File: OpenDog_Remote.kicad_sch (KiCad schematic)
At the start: 37 parts, among them J1 Conn_01x03_Pin, J10 Conn_01x03_Pin, J11 Conn_01x03_Pin, J12 Conn_01x02_Pin, J13 Conn_01x03_Pin, J14 Conn_01x03_Pin, J15 Conn_01x03_Pin, J16 Conn_01x03_Pin, J17 NRF, J18 Conn_02x08_Odd_Even, J2 Conn_01x03_Pin, J3 Conn_01x03_Pin, J4 Conn_01x03_Pin, J5 Conn_01x03_Pin, J6 Conn_01x03_Pin, J7 Conn_01x14, J8 Conn_01x03_Pin, J9 Conn_01x03_Pin, U1 Teensy4.1

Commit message: Added JLCPCB part #, round some board corners.
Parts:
- J1, J10, J11, J13, J14, J15, J16, J2, J3, J4, J5, J6, J8, J9: JLC Part # (none) -> C722693
- J12: JLC Part # (none) -> C2908596
- J18: JLC Part # (none) -> C92267
- J7: JLC Part # (none) -> C225266
- R1, R10, R11, R12, R13, R2, R3, R4, R5, R6, R7, R8, R9: JLC Part # (none) -> C25744
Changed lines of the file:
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@@
+      (effects (font (size 1.27 1.27)) hide)
+    )
+    (property "JLC Part #" "C722693" (at 66.04 149.225 0)
       (effects (font (size 1.27 1.27)) hide)
     )
@@
       (effects (font (size 1.27 1.27)) hide)
     )
+    (property "JLC Part #" "C25744" (at 90.17 139.7 0)
+      (effects (font (size 1.27 1.27)) hide)
+    )
     (pin "1")
     (pin "2")
@@
       (effects (font (size 1.27 1.27)) hide)
     )
+    (property "JLC Part #" "C722693" (at 207.01 44.45 0)
+      (effects (font (size 1.27 1.27)) hide)
+    )
     (pin "1")
     (pin "2")
@@
       (effects (font (size 1.27 1.27)) hide)
     )
+    (property "JLC Part #" "C25744" (at 88.9 173.99 0)
+      (effects (font (size 1.27 1.27)) hide)
+    )
     (pin "1")
     (pin "2")
@@
       (effects (font (size 1.27 1.27)) hide)
     )
+    (property "JLC Part #" "C25744" (at 55.245 173.99 0)
+      (effects (font (size 1.27 1.27)) hide)
+    )
     (pin "1")
     (pin "2")
@@
       (effects (font (size 1.27 1.27)) hide)
     )
+    (property "JLC Part #" "C25744" (at 152.4 173.99 0)
+      (effects (font (size 1.27 1.27)) hide)
+    )
     (pin "1")
     (pin "2")
@@
       (effects (font (size 1.27 1.27)) hide)
     )
+    (property "JLC Part #" "C25744" (at 121.92 139.7 0)
+      (effects (font (size 1.27 1.27)) hide)
+    )
     (pin "1")
     (pin "2")
@@
       (effects (font (size 1.27 1.27)) hide)
     )
+    (property "JLC Part #" "C25744" (at 122.555 182.88 0)
+      (effects (font (size 1.27 1.27)) hide)
+    )
     (pin "1")
     (pin "2")
@@
       (effects (font (size 1.27 1.27)) hide)
     )
+    (property "JLC Part #" "C722693" (at 206.375 99.06 0)
+      (effects (font (size 1.27 1.27)) hide)
+    )
     (pin "1")
     (pin "2")
@@
       (effects (font (size 1.27 1.27)) hide)
     )
+    (property "JLC Part #" "C722693" (at 134.62 181.61 0)
+      (effects (font (size 1.27 1.27)) hide)
+    )
     (pin "1")
     (pin "2")
@@
     )
     (property "Datasheet" "~" (at 36.195 48.26 0)
+      (effects (font (size 1.27 1.27)) hide)
+    )
+    (property "JLC Part #" "C92267" (at 36.195 48.26 0)
       (effects (font (size 1.27 1.27)) hide)
     )
@@
       (effects (font (size 1.27 1.27)) hide)
     )
+    (property "JLC Part #" "C722693" (at 206.375 90.805 0)
+      (effects (font (size 1.27 1.27)) hide)
+    )
     (pin "1")
     (pin "2")
@@
       (effects (font (size 1.27 1.27)) hide)
     )
+    (property "JLC Part #" "C25744" (at 55.245 182.88 0)
+      (effects (font (size 1.27 1.27)) hide)
+    )
     (pin "1")
     (pin "2")
@@
       (effects (font (size 1.27 1.27)) hide)
     )
+    (property "JLC Part #" "C25744" (at 26.035 140.97 0)
+      (effects (font (size 1.27 1.27)) hide)
+    )
     (pin "1")
     (pin "2")
@@
       (effects (font (size 1.27 1.27)) hide)
     )
+    (property "JLC Part #" "C25744" (at 58.42 140.335 0)
+      (effects (font (size 1.27 1.27)) hide)
+    )
     (pin "1")
     (pin "2")
@@
       (effects (font (size 1.27 1.27)) hide)
     )
+    (property "JLC Part #" "C722693" (at 129.54 148.59 0)
+      (effects (font (size 1.27 1.27)) hide)
+    )
     (pin "1")
     (pin "2")
@@
     )
     (property "Datasheet" "~" (at 97.79 148.59 0)
+      (effects (font (size 1.27 1.27)) hide)
+    )
+    (property "JLC Part #" "C722693" (at 97.79 148.59 0)
       (effects (font (size 1.27 1.27)) hide)
     )
@@
       (effects (font (size 1.27 1.27)) hide)
     )
+    (property "JLC Part #" "C722693" (at 33.655 149.86 0)
+      (effects (font (size 1.27 1.27)) hide)
+    )
     (pin "1")
     (pin "2")
@@
     )
     (property "Datasheet" "~" (at 201.295 131.445 0)
+      (effects (font (size 1.27 1.27)) hide)
+    )
+    (property "JLC Part #" "C225266" (at 201.295 131.445 0)
       (effects (font (size 1.27 1.27)) hide)
     )
@@
       (effects (font (size 1.27 1.27)) hide)
     )
+    (property "JLC Part #" "C722693" (at 206.375 82.55 0)
+      (effects (font (size 1.27 1.27)) hide)
+    )
     (pin "1")
     (pin "2")
@@
       (effects (font (size 1.27 1.27)) hide)
     )
+    (property "JLC Part #" "C722693" (at 67.31 181.61 0)
+      (effects (font (size 1.27 1.27)) hide)
+    )
     (pin "1")
     (pin "2")
@@
       (effects (font (size 1.27 1.27)) hide)
     )
+    (property "JLC Part #" "C722693" (at 31.75 180.34 0)
+      (effects (font (size 1.27 1.27)) hide)
+    )
     (pin "1")
     (pin "2")
@@
       (effects (font (size 1.27 1.27)) hide)
     )
+    (property "JLC Part #" "C722693" (at 207.01 60.96 0)
+      (effects (font (size 1.27 1.27)) hide)
+    )
     (pin "1")
     (pin "2")
@@
     )
     (property "Datasheet" "~" (at 19.685 172.72 0)
+      (effects (font (size 1.27 1.27)) hide)
+    )
+    (property "JLC Part #" "C25744" (at 19.685 172.72 0)
       (effects (font (size 1.27 1.27)) hide)
     )
@@
       (effects (font (size 1.27 1.27)) hide)
     )
+    (property "JLC Part #" "C25744" (at 122.555 173.99 0)
+      (effects (font (size 1.27 1.27)) hide)
+    )
     (pin "1")
     (pin "2")
@@
     )
     (property "Datasheet" "~" (at 19.685 181.61 0)
+      (effects (font (size 1.27 1.27)) hide)
+    )
+    (property "JLC Part #" "C25744" (at 19.685 181.61 0)
       (effects (font (size 1.27 1.27)) hide)
     )
@@
     )
     (property "Datasheet" "~" (at 163.195 184.15 0)
+      (effects (font (size 1.27 1.27)) hide)
+    )
+    (property "JLC Part #" "C2908596" (at 163.195 184.15 0)
       (effects (font (size 1.27 1.27)) hide)
     )
@@
       (effects (font (size 1.27 1.27)) hide)
     )
+    (property "JLC Part #" "C25744" (at 88.9 182.88 0)
+      (effects (font (size 1.27 1.27)) hide)
+    )
     (pin "1")
     (pin "2")
@@
       (effects (font (size 1.27 1.27)) hide)
     )
+    (property "JLC Part #" "C722693" (at 207.01 52.705 0)
+      (effects (font (size 1.27 1.27)) hide)
+    )
     (pin "1")
     (pin "2")
@@
       (effects (font (size 1.27 1.27)) hide)
     )
+    (property "JLC Part #" "C722693" (at 100.965 181.61 0)
+      (effects (font (size 1.27 1.27)) hide)
+    )

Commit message: Update JPC part #s.
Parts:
- J12: JLC Part # C2908596 -> C2979476
- J7: JLC Part # C225266 -> C2905490
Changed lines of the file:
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@@
       (effects (font (size 1.27 1.27)) hide)
     )
-    (property "JLC Part #" "C225266" (at 201.295 131.445 0)
+    (property "JLC Part #" "C2905490" (at 201.295 131.445 0)
       (effects (font (size 1.27 1.27)) hide)
     )
@@
       (effects (font (size 1.27 1.27)) hide)
     )
-    (property "JLC Part #" "C2908596" (at 163.195 184.15 0)
-      (effects (font (size 1.27 1.27)) hide)
-    )
+    (property "JLC Part #" "C2979476" (at 163.195 184.15 0)
+      (effects (font (size 1.27 1.27)) hide)
+    )

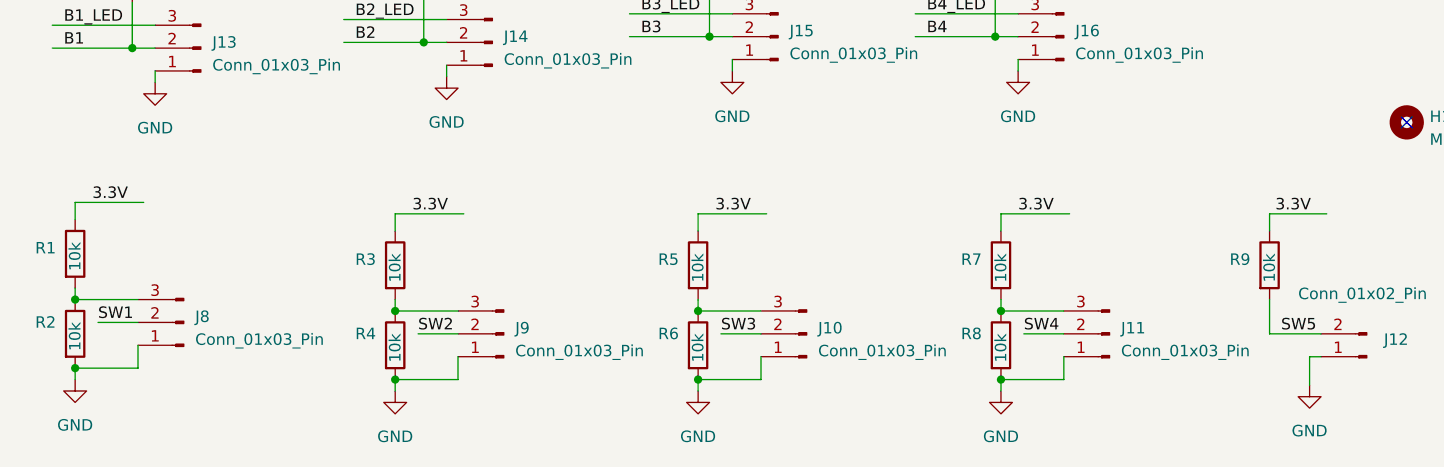
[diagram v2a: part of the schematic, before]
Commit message: Update the OpenDog remote board.
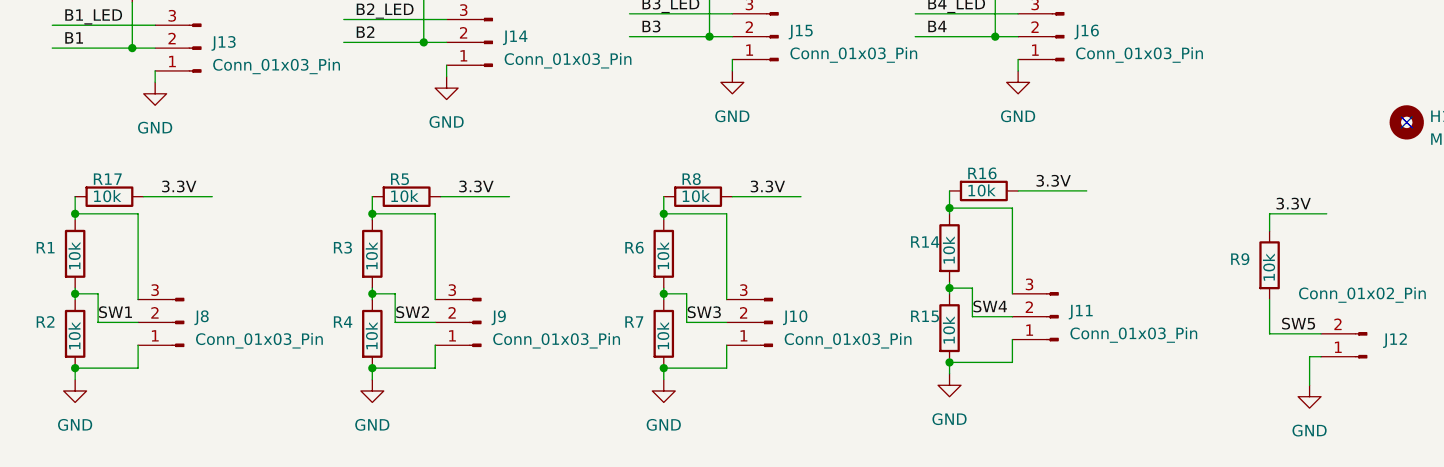
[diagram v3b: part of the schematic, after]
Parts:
- added R14, R15, R16, R17: 10k, Resistor_SMD:R_0402_1005Metric, symbol Device:R
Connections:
- net 3.3V: now also R8.1, R16.1, R17.1; no longer R1.1, R3.1, R7.1
- net GND: now also R7.2, R15.2; no longer R6.2, R8.2
- net SW1: now also R1.2, R2.1
- net SW2: now also R3.2, R4.1
- net SW3: now also R6.2, R7.1
- net SW4: now also R14.2, R15.1
- net at J10.3 (Pin_3), R6.1: now also R8.2; no longer R5.2
- new net: J9.3 (Pin_3), R3.1, R5.2
- new net: J8.3 (Pin_3), R1.1, R17.2
- new net: J11.3 (Pin_3), R14.1, R16.2

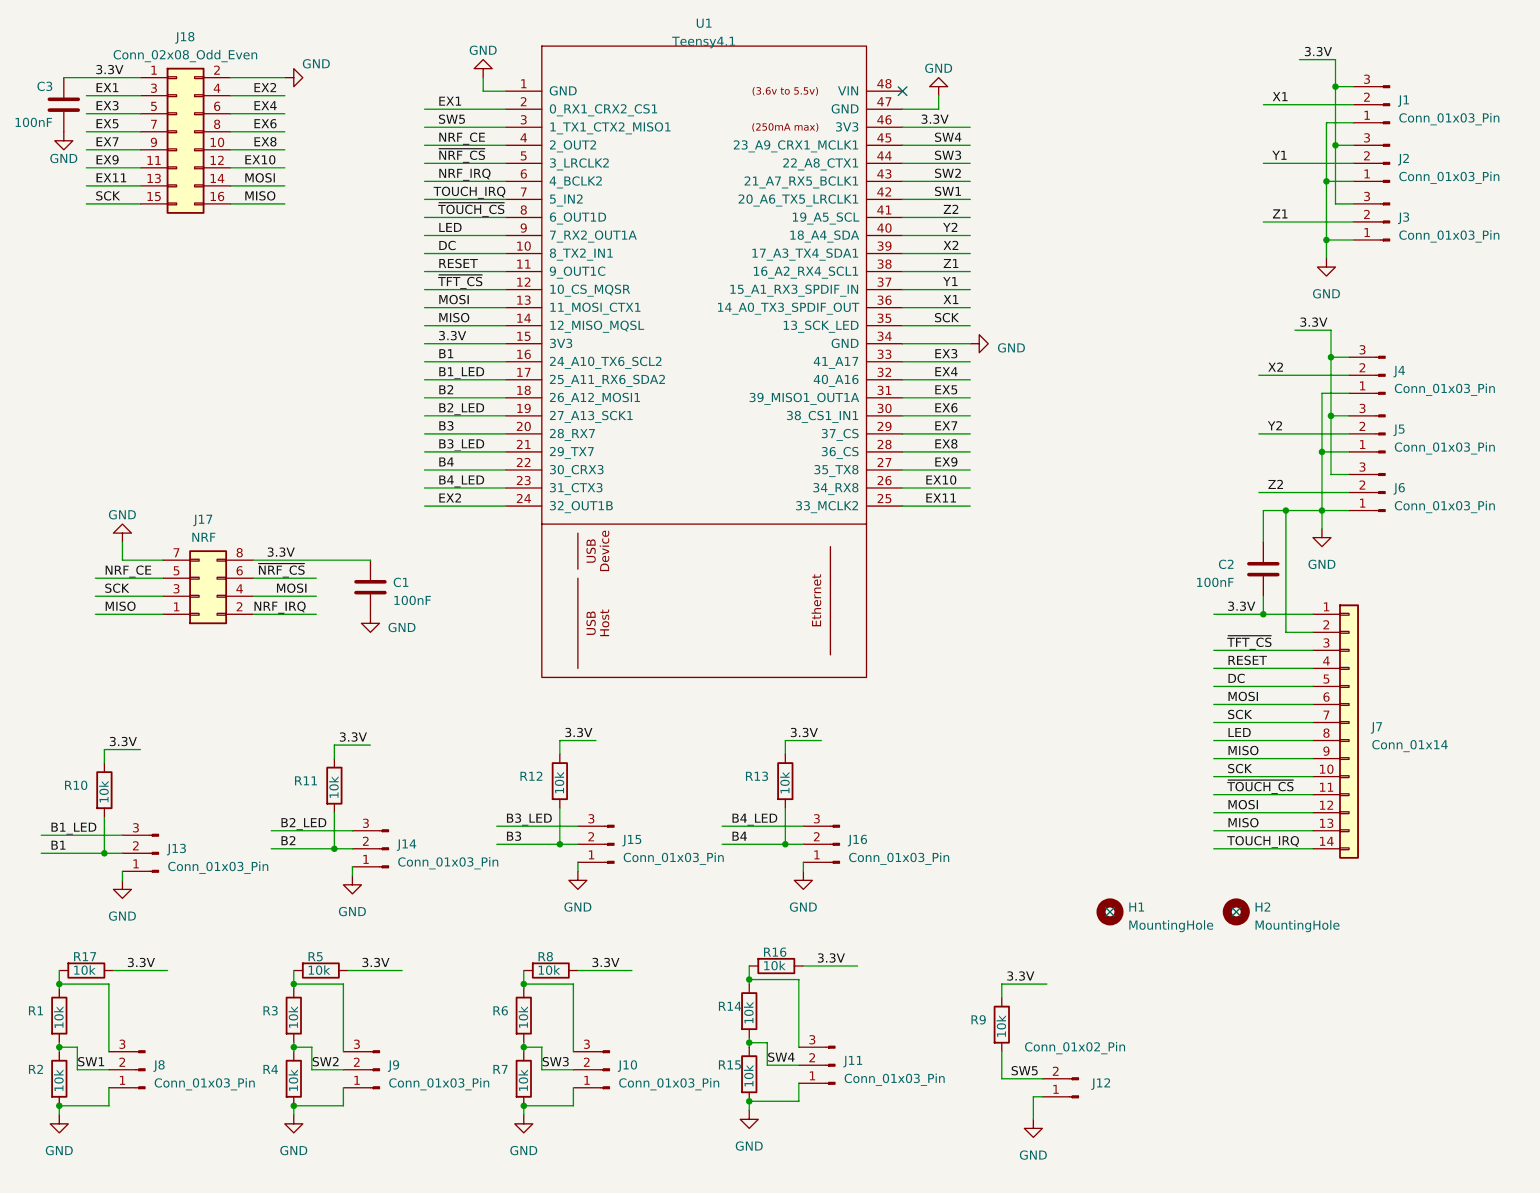
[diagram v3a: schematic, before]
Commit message: Add filtering caps on the switches and pots.
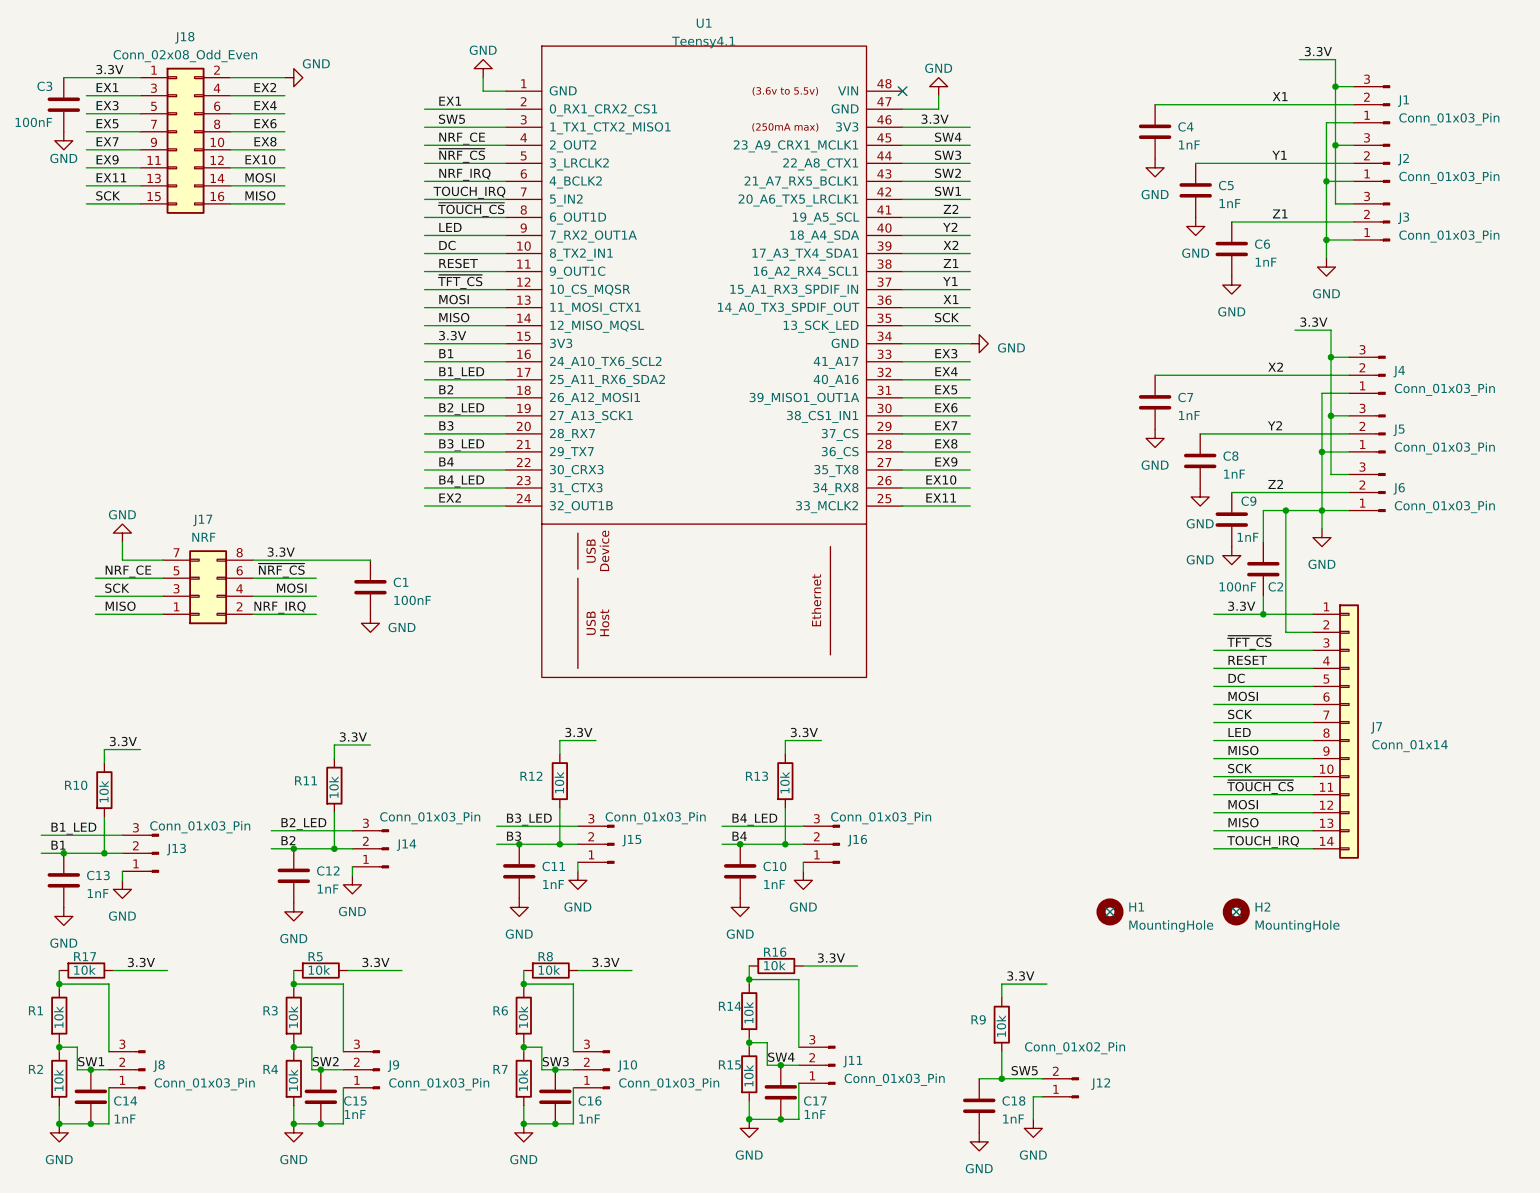
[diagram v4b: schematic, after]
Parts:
- added C10, C11, C12, C13, C14, C15, C16, C17, C18, C4, C5, C6, C7, C8, C9: 1nF, Capacitor_SMD:C_0402_1005Metric, symbol Device:C
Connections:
- net B1: now also C13.1
- net B2: now also C12.1
- net B3: now also C11.1
- net B4: now also C10.1
- net GND: now also C10.2, C11.2, C12.2, C13.2, C14.2, C15.2, C16.2, C17.2, C18.2, C4.2, C5.2, C6.2, C7.2, C8.2, C9.2
- net SW1: now also C14.1
- net SW2: now also C15.1
- net SW3: now also C16.1
- net SW4: now also C17.1
- net SW5: now also C18.1
- net X1: now also C4.1
- net X2: now also C7.1
- net Y1: now also C5.1
- net Y2: now also C8.1
- net Z1: now also C6.1
- net Z2: now also C9.1
